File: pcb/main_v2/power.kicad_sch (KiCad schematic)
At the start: 36 parts, among them IC201 AP22811AW5-7, Q201 DMP3068L-7, SW201 SW_DIP_x01, U201 LT3042xMSE

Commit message: update bom
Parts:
- added J201: Barrel_Jack, Connector_BarrelJack:BarrelJack_CUI_PJ-063AH_Horizontal_CircularHoles, symbol Connector:Barrel_Jack
- renumbered C208 to C203, C203 to C204, C204 to C205, C205 to C206, C206 to C207, C207 to C208, D204 to D203, D203 to D204, R206 to R201, R211 to R202, R201 to R203, R202 to R205, R203 to R206, R205 to R207, R207 to R208, R208 to R209, R209 to R210, R210 to R211
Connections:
- net GND: now also J201.2
- net DC Power: no longer names the net of D201.1 (K), Q201.3 (D), TP201.1
- net DC Power: now also J201.1
- net USB Power renamed Power Raw
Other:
- note added: "Enble with pin AND Switch"
- note removed: "Enble via pin AND Switch"
- moved on the sheet: C202, C203, D201, D204, FB201, Q201, R202, R205, TP201

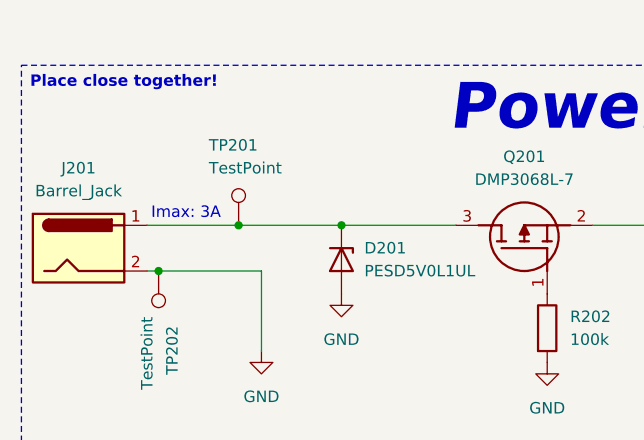
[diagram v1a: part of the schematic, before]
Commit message: updated layout
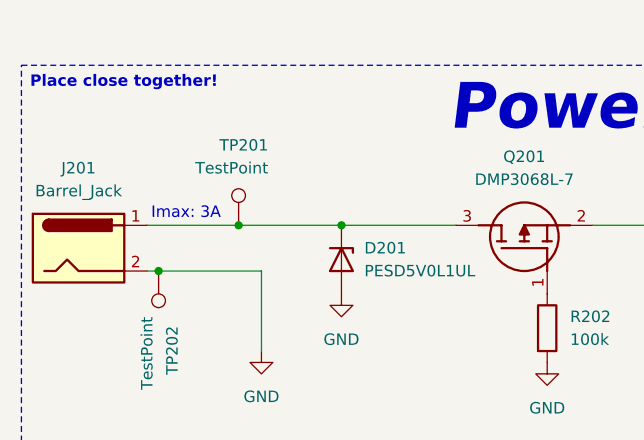
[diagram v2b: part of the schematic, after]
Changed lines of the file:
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@@
 		(lib_id "Connector:TestPoint")
 		(at 38.1 43.18 0)
+		(mirror y)
 		(unit 1)
 		(body_style 1)
@@
 		(dnp no)
 		(property "Reference" "TP201"
-			(at 34.798 34.29 0)
+			(at 41.402 34.29 0)
 			(show_name no)
 			(do_not_autoplace no)
@@
 		)
 		(property "Value" "TestPoint"
-			(at 34.798 36.83 0)
+			(at 41.402 36.83 0)
 			(show_name no)
 			(do_not_autoplace no)
@@
 		)
 		(property "Footprint" "TestPoint:TestPoint_Pad_D1.0mm"
-			(at 43.18 43.18 0)
+			(at 33.02 43.18 0)
 			(hide yes)
 			(show_name no)
@@
 		)
 		(property "Datasheet" ""
-			(at 43.18 43.18 0)
+			(at 33.02 43.18 0)
 			(hide yes)
 			(show_name no)

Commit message: finished layout
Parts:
- added R213: 100k, Resistor_SMD:R_0603_1608Metric, symbol Device:R
- added TP206: TestPoint, TestPoint:TestPoint_Pad_D1.0mm, symbol Connector:TestPoint
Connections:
- net GND: now also R213.1, TP206.1
- net at D204.2 (A), IC201.4 (EN), SW201.2: now also R213.2
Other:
- note added: "Enble the LM with IO pin AND Switch!"
- note removed: "Enble with pin AND Switch"
- moved on the sheet: R201, SW201

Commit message: update do docs and minor layout fix
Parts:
- added TP207, TP208: TestPoint, TestPoint:TestPoint_Pad_D1.0mm, symbol Connector:TestPoint
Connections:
- net +5V: now also TP207.1
- net GND: now also TP208.1

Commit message: added new doc files
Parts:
- D201: value PESD5V0L1UL -> DESD5V0U1BL-7B
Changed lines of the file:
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@@
 			)
 		)
-		(property "Value" "PESD5V0L1UL"
+		(property "Value" "DESD5V0U1BL-7B"
 			(at 52.07 48.2599 90)
 			(show_name no)
@@
 			)
 		)
-		(property "Datasheet" "https://assets.nexperia.com/documents/data-sheet/PESD5V0L1UL.pdf"
+		(property "Datasheet" ""
 			(at 54.61 46.99 0)
 			(hide yes)

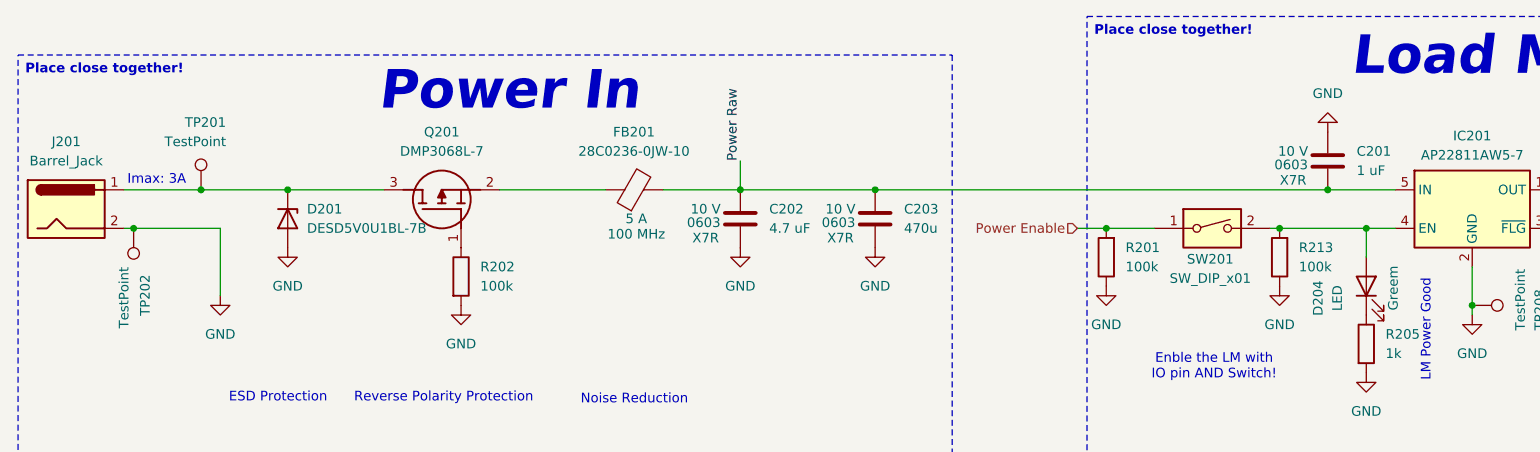
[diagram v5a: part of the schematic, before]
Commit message: updated project after assembly
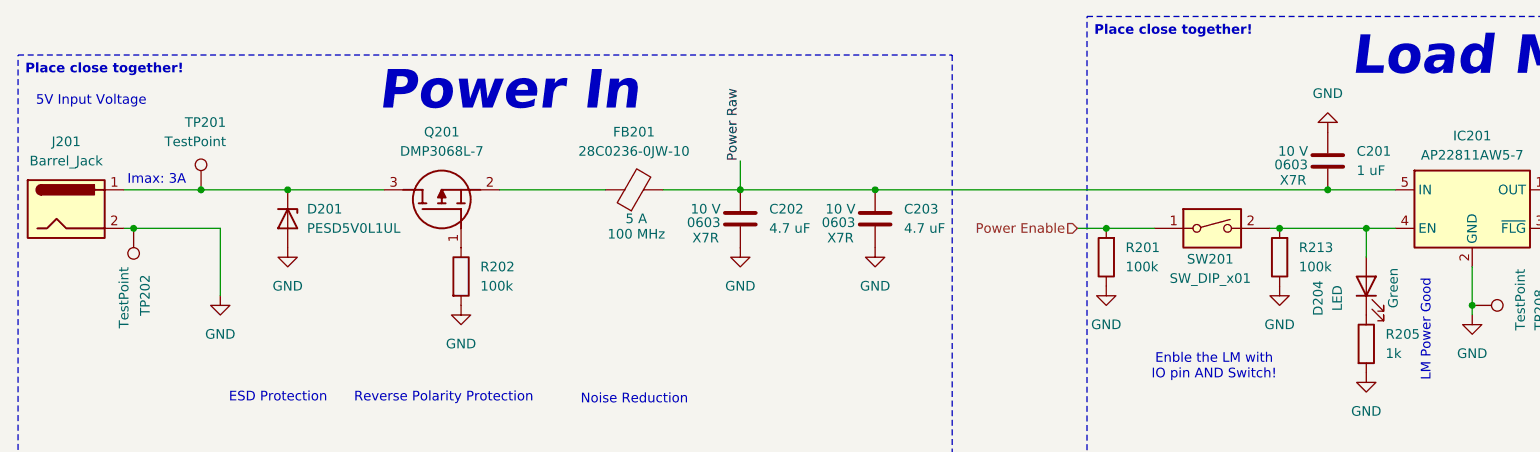
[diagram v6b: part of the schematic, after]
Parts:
- C203: value 470u -> 4.7 uF
- D201: value DESD5V0U1BL-7B -> PESD5V0L1UL
- D204: Color Greem -> Green
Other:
- note added: "5V Input Voltage"
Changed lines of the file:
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@@
 		)
 	)
+	(text "5V Input Voltage"
+		(exclude_from_sim no)
+		(at 23.622 31.496 0)
+		(effects
+			(font
+				(size 1.27 1.27)
+			)
+		)
+	)
 	(text_box "Place close together!"
 		(exclude_from_sim no)
@@
 			)
 		)
-		(property "Value" "DESD5V0U1BL-7B"
+		(property "Value" "PESD5V0L1UL"
 			(at 52.07 48.2599 90)
 			(show_name no)
@@
 			)
 		)
-		(property "Datasheet" ""
+		(property "Datasheet" "https://assets.nexperia.com/documents/data-sheet/PESD5V0L1UL.pdf"
 			(at 54.61 46.99 0)
 			(hide yes)
@@
 			)
 		)
-		(property "Value" "470u"
+		(property "Value" "4.7 uF"
 			(at 130.81 48.2599 0)
 			(show_name no)
@@
 			)
 		)
-		(property "Color" "Greem"
+		(property "Color" "Green"
 			(at 195.326 56.134 0)
 			(show_name no)
